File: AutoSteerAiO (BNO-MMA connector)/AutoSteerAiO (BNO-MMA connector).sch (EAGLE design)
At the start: 86 parts, among them J4 CONNECTOR 1x5 PINS, K4 CB1A-P-12V, T1 BC547, U1 VX7805-1000

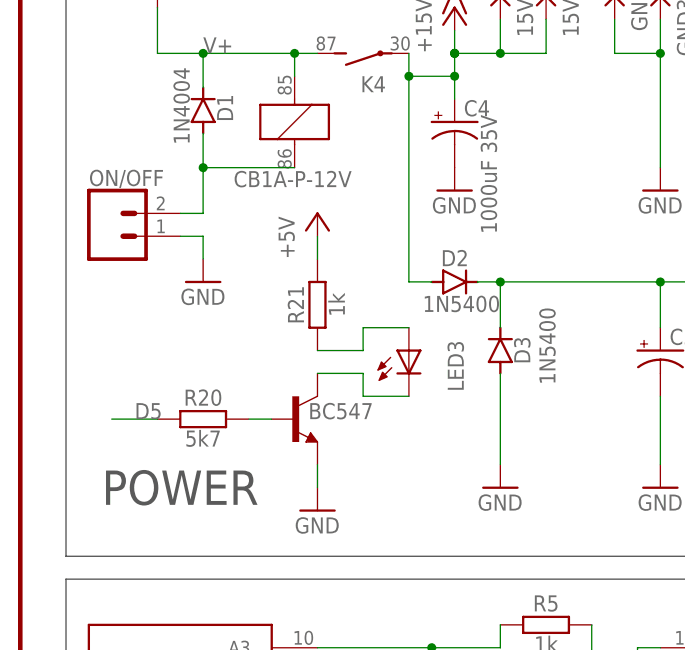
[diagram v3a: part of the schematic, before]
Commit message: Add files via upload
Added diode D6 to protect from reverse polarity
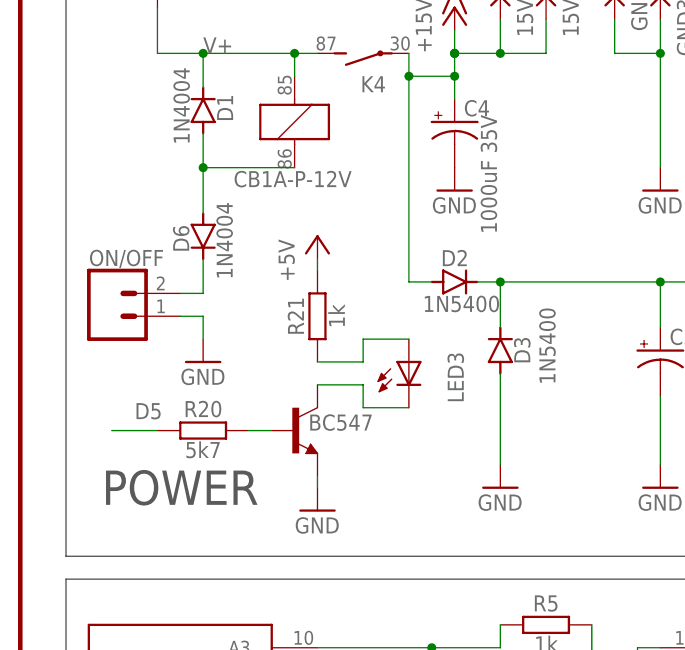
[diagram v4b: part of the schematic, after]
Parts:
- added D6: 1N4004, diode:1N4004
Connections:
- new net N$28: D6.C, ON/OFF.2
- net N$5: now also D6.A; no longer ON/OFF.2
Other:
- moved on the sheet: LED3, ON/OFF, R20, R21
